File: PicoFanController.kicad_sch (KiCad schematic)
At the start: 58 parts, among them J1 Dell Fan, J10 Conn_01x05_Pin, J11 Conn_01x05_Pin, J12 Conn_01x05_Pin, J13 Conn_01x05_Pin, J14 Conn_01x05_Pin, J15 Conn_01x05_Pin, J2 Power, J3 USB_C_Receptacle_USB2.0_16P, J4 Power Select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

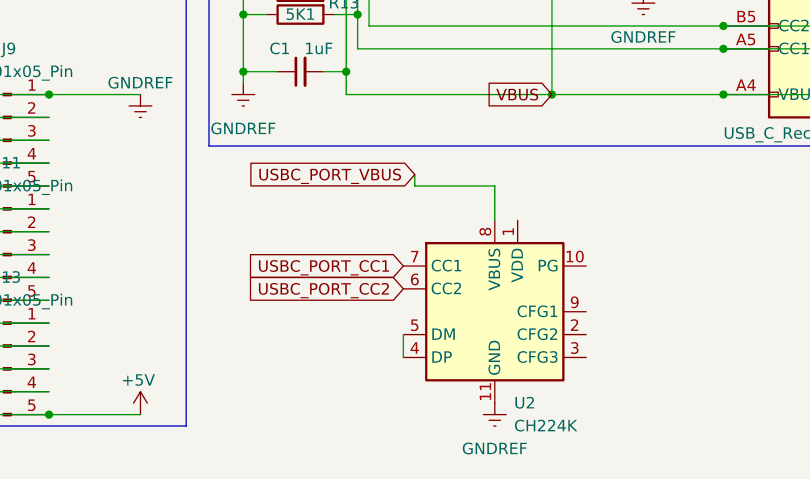
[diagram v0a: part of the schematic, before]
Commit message: Postponed the refactor
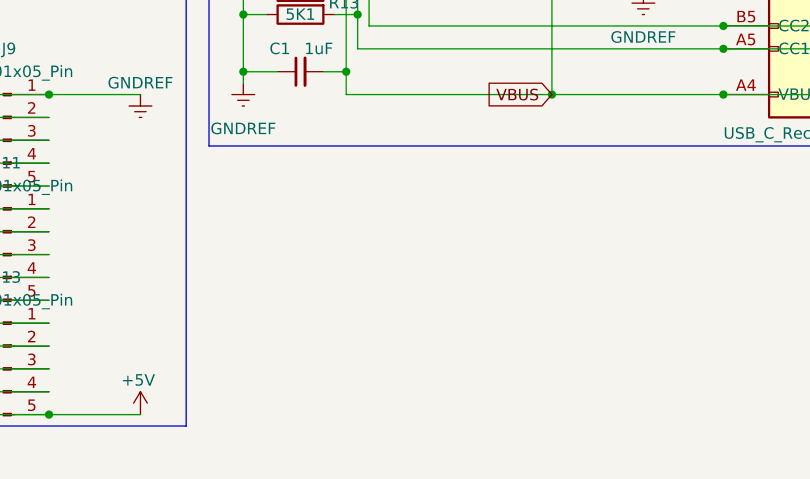
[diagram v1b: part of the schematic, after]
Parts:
- removed U2: CH224K, Package_SO:SSOP-10-1EP_3.9x4.9mm_P1mm_EP2.1x3.3mm, symbol Interface_USB:CH224K
